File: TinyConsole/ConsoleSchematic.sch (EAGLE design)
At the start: 8 parts, among them J1 POWER_JACKPTH, U1 JOYSTICKPTH, U2 TINY85-20-DIP

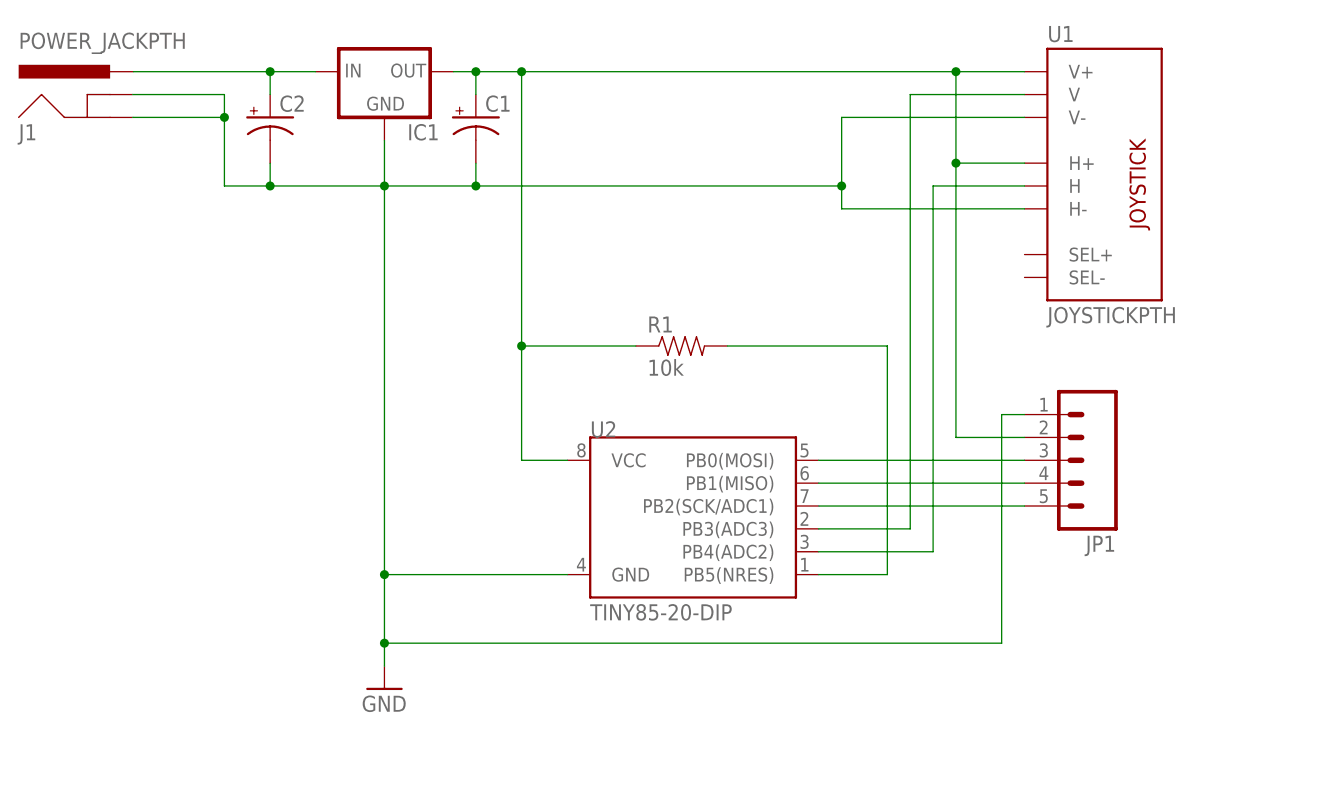
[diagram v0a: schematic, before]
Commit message: TinyConsole: Finished routing PCB.
I've now added an LED + Resistor, along with headers for the programmer.
I also checked the pin outs against the actual pin outs for the display
and I believe it now lines up correctly.  In short, I think it's good to
go!!!
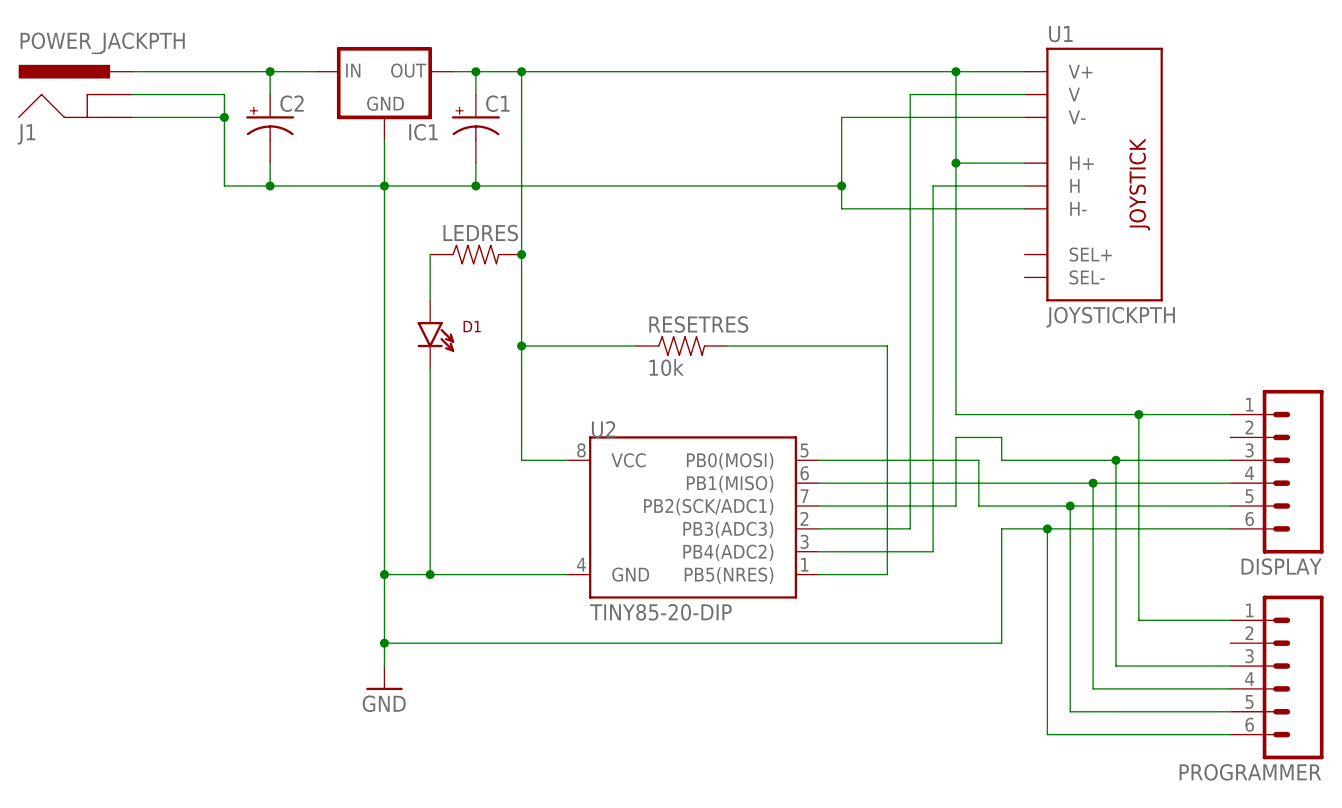
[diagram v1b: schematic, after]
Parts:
- removed JP1: (no value), SparkFun-Connectors:M05LOCK
- added D1: (no value), SparkFun-LED:LTE-302
- added DISPLAY, PROGRAMMER: (no value), SparkFun-Connectors:M06SILK_FEMALE_PTH
- added LEDRES: (no value), SparkFun-Passives:RESISTOREZ
- renumbered R1 to RESETRES
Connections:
- removed net N$5: JP1.5, U2.PB2(SCK/ADC1)
- removed net N$6: JP1.4, U2.PB1(MISO)
- removed net N$7: JP1.3, U2.PB0(MOSI)
- new net CS: DISPLAY.4, PROGRAMMER.4, U2.PB1(MISO)
- new net MOSI: DISPLAY.5, PROGRAMMER.5, U2.PB0(MOSI)
- new net SCK: DISPLAY.3, PROGRAMMER.3, U2.PB2(SCK/ADC1)
- new net VCC: C1.+, DISPLAY.1, IC1.OUT, LEDRES.2, PROGRAMMER.1, RESETRES.1, U1.H+, U1.V+, U2.VCC
- net GND: now also D1.C, DISPLAY.6, PROGRAMMER.6; no longer JP1.1
- net N$1: now also D1.A, LEDRES.1; no longer C1.+, IC1.OUT, JP1.2, RESETRES.1, U1.H+, U1.V+, U2.VCC
